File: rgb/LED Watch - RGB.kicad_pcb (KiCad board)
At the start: 4 copper layers, 42.9 x 50.3 mm, 146 parts, among them J1 AVR-ISP-6, J2 Lipo, J3 Coin Cell, SW1 SW_DPST, SW2 SW_DPST, U10 B39D3RGB-F6C0001HOU1930, U100 B39D3RGB-F6C0001HOU1930, U101 B39D3RGB-F6C0001HOU1930, U102 B39D3RGB-F6C0001HOU1930, U103 B39D3RGB-F6C0001HOU1930, U104 B39D3RGB-F6C0001HOU1930, U105 B39D3RGB-F6C0001HOU1930, U106 B39D3RGB-F6C0001HOU1930, U107 B39D3RGB-F6C0001HOU1930, U108 B39D3RGB-F6C0001HOU1930, U109 B39D3RGB-F6C0001HOU1930, U11 B39D3RGB-F6C0001HOU1930, U110 B39D3RGB-F6C0001HOU1930, U111 B39D3RGB-F6C0001HOU1930, U112 B39D3RGB-F6C0001HOU1930, U113 B39D3RGB-F6C0001HOU1930, U114 B39D3RGB-F6C0001HOU1930, U115 B39D3RGB-F6C0001HOU1930, U116 B39D3RGB-F6C0001HOU1930, U117 B39D3RGB-F6C0001HOU1930, U118 B39D3RGB-F6C0001HOU1930, U119 B39D3RGB-F6C0001HOU1930, U12 B39D3RGB-F6C0001HOU1930, U120 B39D3RGB-F6C0001HOU1930, U121 B39D3RGB-F6C0001HOU1930, U122 B39D3RGB-F6C0001HOU1930, U123 B39D3RGB-F6C0001HOU1930, U124 B39D3RGB-F6C0001HOU1930, U125 B39D3RGB-F6C0001HOU1930, U126 B39D3RGB-F6C0001HOU1930, U127 B39D3RGB-F6C0001HOU1930, U128 B39D3RGB-F6C0001HOU1930, U129 B39D3RGB-F6C0001HOU1930, U13 B39D3RGB-F6C0001HOU1930, U130 B39D3RGB-F6C0001HOU1930, U131 B39D3RGB-F6C0001HOU1930, U132 B39D3RGB-F6C0001HOU1930, U133 B39D3RGB-F6C0001HOU1930, U134 BMI160, U135 ATmega165PA-M, U14 B39D3RGB-F6C0001HOU1930, U15 B39D3RGB-F6C0001HOU1930, U16 B39D3RGB-F6C0001HOU1930, U17 B39D3RGB-F6C0001HOU1930, U18 B39D3RGB-F6C0001HOU1930, U19 B39D3RGB-F6C0001HOU1930, U2 B39D3RGB-F6C0001HOU1930, U20 B39D3RGB-F6C0001HOU1930, U21 B39D3RGB-F6C0001HOU1930, U22 B39D3RGB-F6C0001HOU1930, U23 B39D3RGB-F6C0001HOU1930, U24 B39D3RGB-F6C0001HOU1930, U25 B39D3RGB-F6C0001HOU1930, U26 B39D3RGB-F6C0001HOU1930, U27 B39D3RGB-F6C0001HOU1930, U28 B39D3RGB-F6C0001HOU1930, U29 B39D3RGB-F6C0001HOU1930, U3 B39D3RGB-F6C0001HOU1930, U30 B39D3RGB-F6C0001HOU1930, U31 B39D3RGB-F6C0001HOU1930, U32 B39D3RGB-F6C0001HOU1930, U33 B39D3RGB-F6C0001HOU1930, U34 B39D3RGB-F6C0001HOU1930, U35 B39D3RGB-F6C0001HOU1930, U36 B39D3RGB-F6C0001HOU1930, U37 B39D3RGB-F6C0001HOU1930, U38 B39D3RGB-F6C0001HOU1930, U39 B39D3RGB-F6C0001HOU1930, U4 B39D3RGB-F6C0001HOU1930, U40 B39D3RGB-F6C0001HOU1930, U41 B39D3RGB-F6C0001HOU1930, U42 B39D3RGB-F6C0001HOU1930, U43 B39D3RGB-F6C0001HOU1930, U44 B39D3RGB-F6C0001HOU1930, U45 B39D3RGB-F6C0001HOU1930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

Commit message: rgb: the live RGB work (Oct 2026 edits) becomes the main "LED Watch - RGB" project; add fab-rfq 2026-10-05, snapshots, Rhino layout
- rgb/LED Watch - RGB.* = the files from the working folder as of 2026-10-14 (board routes with 0 unconnected nets); the December 2025 version that the repository had is kept in rgb/archive/pre-claude/2025-12-08 ...
- rgb/production/fab-rfq 2026-10-05/ (BOM, placement files, Gerbers, DRC, quote screenshots, notes), rgb/archive/pre-claude/2026-10-05 snapshots ..., rgb/mechanical/watch layout 1.3dm
- updated KiCad project/layout state files of the archived variants from the working folder
- .gitignore: _old-desktop-copies/ (the previous loose Desktop copies, kept untouched next to the repository)

Co-Authored-By: Claude Sonnet 5.5 <noreply@anthropic.com>
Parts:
- U134: value BMI160 -> BMI270
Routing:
- net Net-(J1-VCC): track 42.8 -> 44.7 mm, vias 9 -> 11
- net /Minute6: track 32.9 -> 34.6 mm, vias 7 -> 8
- net Net-(J1-GND): vias 3 -> 7

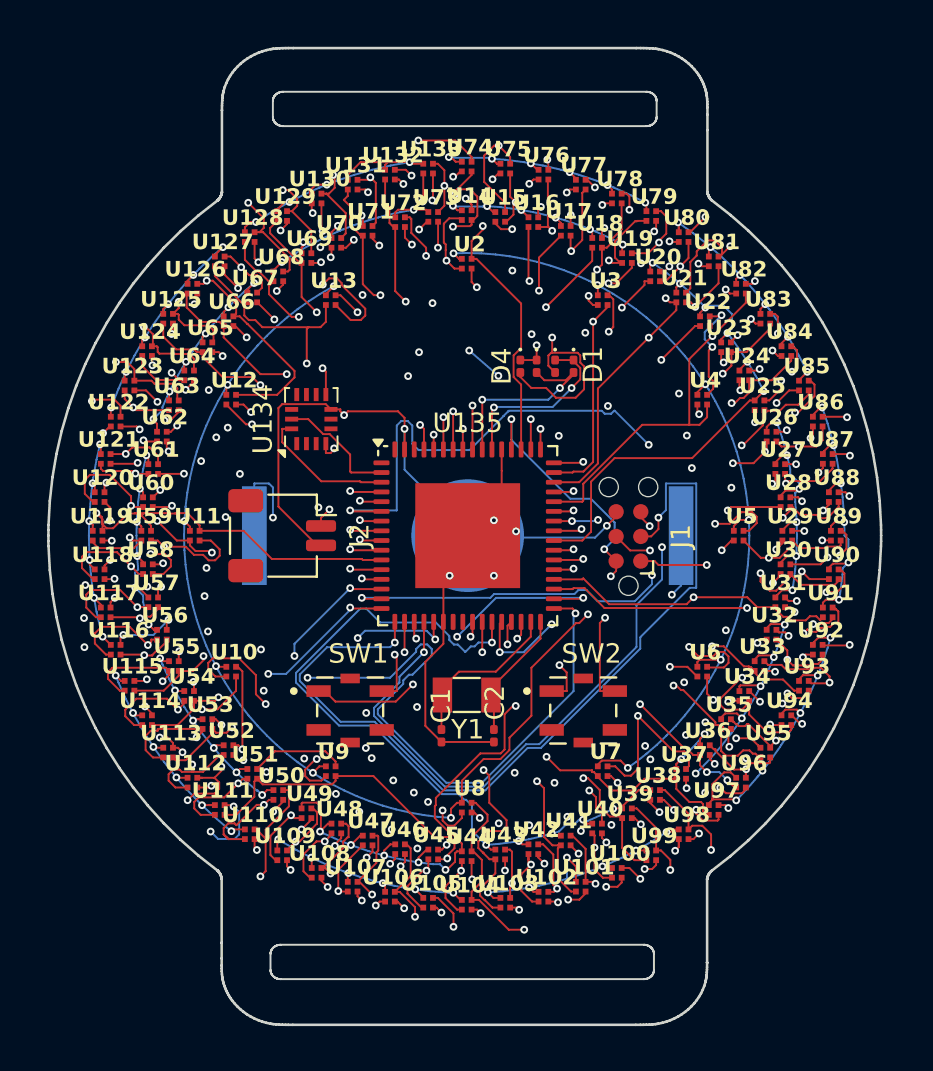
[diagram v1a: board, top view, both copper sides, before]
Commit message: rgb: the new RGB design takes over 'LED Watch - RGB'; the old routed RGB board (Harvatek, ATmega165PA) moves to rgb/archive; no 'v2' naming
Co-Authored-By: Claude Sonnet 5.5 <noreply@anthropic.com>
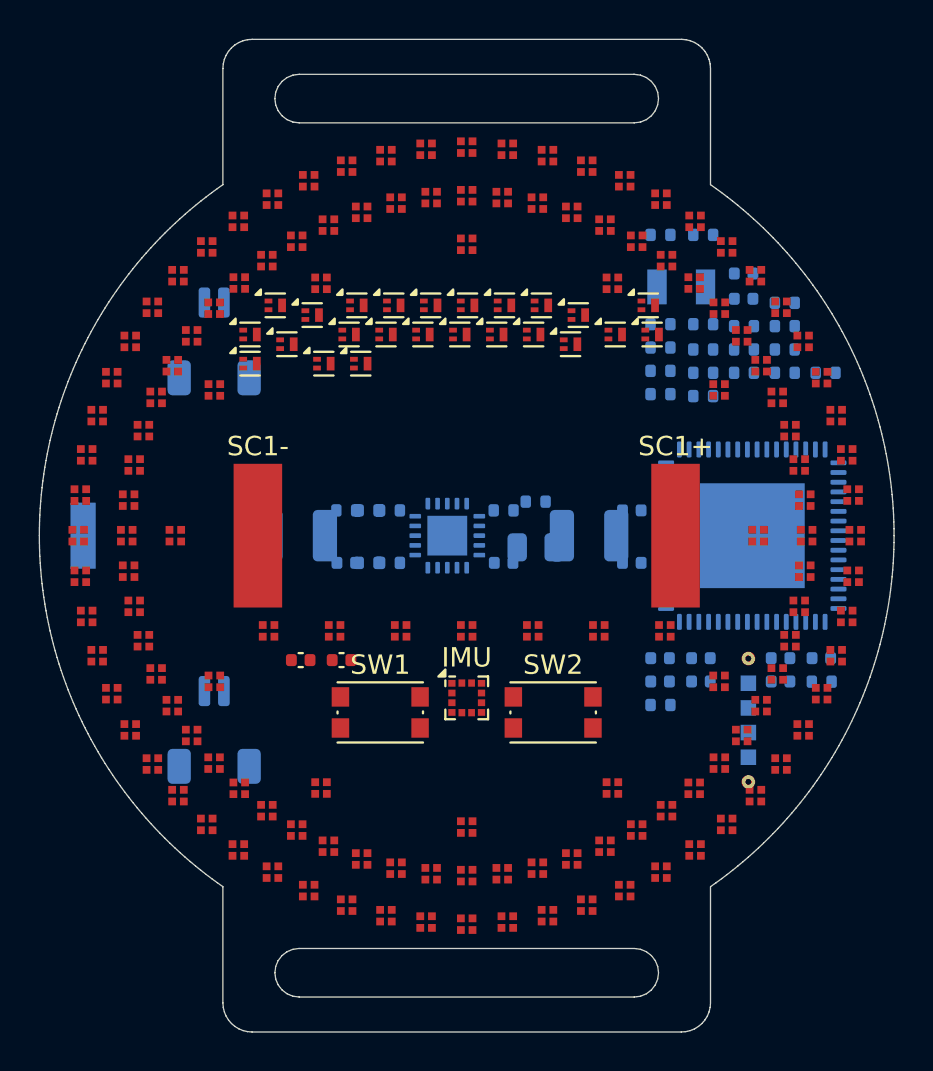
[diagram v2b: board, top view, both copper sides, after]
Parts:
- removed C1, C2: C, Capacitor_SMD:C_0201_0603Metric
- removed D1, D2, D3, D4: LED, LED_SMD:LED_0201_0603Metric
- removed J3: Coin Cell, Battery:BatteryHolder_Keystone_3034_1x20mm
- removed U134: BMI270, Package_LGA:Bosch_LGA-14_3x2.5mm_P0.5mm
- removed U135: ATmega165PA-M, Package_DFN_QFN:QFN-64-1EP_9x9mm_P0.5mm_EP5.4x5.4mm
- added BQ: BQ25570, BQ25570RGR_VQFN-20_3.5x3.5mm_P0.5mm_EP2.05mm, B.Cu at (99.0, 100.0)
- added BZ1: PKMCS0909E4000-R1, Piezo_Murata_PKMCS0909E4000-R1_9x9mm, B.Cu at (84.6, 100.0)
- added C20: 18p, C_0402_1005Metric, B.Cu at (114.3, 86.5)
- added C21: 18p, C_0402_1005Metric, B.Cu at (114.3, 87.8)
- added C30: 100n, C_0402_1005Metric, F.Cu at (91.5, 106.4)
- added C31: 100n, C_0402_1005Metric, F.Cu at (93.6, 106.4)
- added C50: 4u7, C_0402_1005Metric, B.Cu at (108.5, 98.7)
- added C51: 10n, C_0402_1005Metric, B.Cu at (93.8, 101.4)
- added C52: 4u7, C_0402_1005Metric, B.Cu at (101.9, 101.4)
- added C53: 10n, C_0402_1005Metric, B.Cu at (108.5, 101.4)
- added C54: 22u, C_0805_2012Metric, B.Cu at (103.5, 100.6)
- added CM1: 100n, C_0402_1005Metric, B.Cu at (110.0, 106.3)
- added CM2: 100n, C_0402_1005Metric, B.Cu at (112.1, 106.3)
- added CM3: 100n, C_0402_1005Metric, B.Cu at (116.2, 106.3)
- added CM4: 100n, C_0402_1005Metric, B.Cu at (118.3, 106.3)
- added CM5: 100n, C_0402_1005Metric, B.Cu at (110.0, 107.5)
- added CM6: 100n, C_0402_1005Metric, B.Cu at (112.1, 107.5)
- added CM7: 100n, C_0402_1005Metric, B.Cu at (116.2, 107.5)
- added IMU: LIS2DW12, LGA-12_2x2mm_P0.5mm, F.Cu at (100.0, 108.3)
- added IND1: NCD0808RGB1 / MHPA0808RGBDT, RGB0808_CommonAnode, F.Cu at (89.8, 104.9)
- added IND2: NCD0808RGB1 / MHPA0808RGBDT, RGB0808_CommonAnode, F.Cu at (93.2, 104.9)
- added IND3: NCD0808RGB1 / MHPA0808RGBDT, RGB0808_CommonAnode, F.Cu at (96.6, 104.9)
- added IND4: NCD0808RGB1 / MHPA0808RGBDT, RGB0808_CommonAnode, F.Cu at (100.0, 104.9)
- added IND5: NCD0808RGB1 / MHPA0808RGBDT, RGB0808_CommonAnode, F.Cu at (103.4, 104.9)
- added IND6: NCD0808RGB1 / MHPA0808RGBDT, RGB0808_CommonAnode, F.Cu at (106.8, 104.9)
- added IND7: NCD0808RGB1 / MHPA0808RGBDT, RGB0808_CommonAnode, F.Cu at (110.2, 104.9)
- added J1B: LiPo, JST_SH_SM02B-SRSS-TB_1x02-1MP_P1.00mm_Horizontal, B.Cu at (87.0, 110.0)
- added L1: 22uH, L_1210_3225Metric, B.Cu at (106.3, 100.0)
- added L2: 10uH, L_1210_3225Metric, B.Cu at (91.3, 100.0)
- added MCU: AVR128DB64-I/MR, VQFN-64-1EP_9x9mm_P0.5mm_EP5.4x5.4mm, B.Cu at (114.7, 100.0)
- added Q1: DMP21D0UFB4, Diodes_DFN1006-3, F.Cu at (90.1, 88.1)
- added Q10: DMP21D0UFB4, Diodes_DFN1006-3, F.Cu at (105.7, 88.6)
- added Q11: DMP21D0UFB4, Diodes_DFN1006-3, F.Cu at (88.8, 89.6)
- added Q12: DMP21D0UFB4, Diodes_DFN1006-3, F.Cu at (93.9, 89.6)
- added Q13: DMP21D0UFB4, Diodes_DFN1006-3, F.Cu at (95.8, 89.6)
- added Q14: DMP21D0UFB4, Diodes_DFN1006-3, F.Cu at (97.7, 89.6)
- added Q15: DMP21D0UFB4, Diodes_DFN1006-3, F.Cu at (99.6, 89.6)
- added Q16: DMP21D0UFB4, Diodes_DFN1006-3, F.Cu at (101.5, 89.6)
- added Q17: DMP21D0UFB4, Diodes_DFN1006-3, F.Cu at (103.4, 89.6)
- added Q18: DMP21D0UFB4, Diodes_DFN1006-3, F.Cu at (107.6, 89.6)
- added Q19: DMP21D0UFB4, Diodes_DFN1006-3, F.Cu at (109.5, 89.6)
- added Q2: DMP21D0UFB4, Diodes_DFN1006-3, F.Cu at (94.3, 88.1)
- added Q20: DMP21D0UFB4, Diodes_DFN1006-3, F.Cu at (90.7, 90.1)
- added Q21: DMP21D0UFB4, Diodes_DFN1006-3, F.Cu at (105.3, 90.1)
- added Q22: DMP21D0UFB4, Diodes_DFN1006-3, F.Cu at (88.8, 91.1)
- added Q23: DMP21D0UFB4, Diodes_DFN1006-3, F.Cu at (92.6, 91.1)
- added Q24: DMP21D0UFB4, Diodes_DFN1006-3, F.Cu at (94.5, 91.1)
- added Q3: DMP21D0UFB4, Diodes_DFN1006-3, F.Cu at (96.2, 88.1)
- added Q4: DMP21D0UFB4, Diodes_DFN1006-3, F.Cu at (98.1, 88.1)
- added Q5: DMP21D0UFB4, Diodes_DFN1006-3, F.Cu at (100.0, 88.1)
- added Q6: DMP21D0UFB4, Diodes_DFN1006-3, F.Cu at (101.9, 88.1)
- added Q7: DMP21D0UFB4, Diodes_DFN1006-3, F.Cu at (103.8, 88.1)
- added Q8: DMP21D0UFB4, Diodes_DFN1006-3, F.Cu at (109.3, 88.1)
- added Q9: DMP21D0UFB4, Diodes_DFN1006-3, F.Cu at (92.0, 88.6)
- added R20: 10k, R_0402_1005Metric, B.Cu at (118.3, 107.5)
- added R21: 10k, R_0402_1005Metric, B.Cu at (110.0, 108.7)
- added R50: 6.49M, R_0402_1005Metric, B.Cu at (96.0, 101.4)
- added R51: 5.11M, R_0402_1005Metric, B.Cu at (95.0, 101.4)
- added R52: 1.47M, R_0402_1005Metric, B.Cu at (96.0, 98.7)
- added R53: 6.49M, R_0402_1005Metric, B.Cu at (103.5, 98.2)
- added R54: 3.74M, R_0402_1005Metric, B.Cu at (101.9, 98.7)
- added R55: 6.49M, R_0402_1005Metric, B.Cu at (93.8, 98.7)
- added R56: 3.74M, R_0402_1005Metric, B.Cu at (95.0, 98.7)
- added RC1: R, R_0402_1005Metric, B.Cu at (110.0, 84.5)
- added RC10: R, R_0402_1005Metric, B.Cu at (114.3, 90.4)
- added RC11: R, R_0402_1005Metric, B.Cu at (116.4, 90.4)
- added RC12: R, R_0402_1005Metric, B.Cu at (110.0, 91.5)
- added RC13: R, R_0402_1005Metric, B.Cu at (112.2, 91.6)
- added RC14: R, R_0402_1005Metric, B.Cu at (114.3, 91.6)
- added RC15: R, R_0402_1005Metric, B.Cu at (116.4, 91.6)
- added RC16: R, R_0402_1005Metric, B.Cu at (118.5, 91.6)
- added RC17: R, R_0402_1005Metric, B.Cu at (110.0, 92.7)
- added RC18: R, R_0402_1005Metric, B.Cu at (112.2, 92.8)
- added RC2: R, R_0402_1005Metric, B.Cu at (112.2, 84.5)
- added RC3: R, R_0402_1005Metric, B.Cu at (116.4, 88.0)
- added RC4: R, R_0402_1005Metric, B.Cu at (110.0, 89.1)
- added RC5: R, R_0402_1005Metric, B.Cu at (112.2, 89.1)
- added RC6: R, R_0402_1005Metric, B.Cu at (114.3, 89.2)
- added RC7: R, R_0402_1005Metric, B.Cu at (116.4, 89.2)
- added RC8: R, R_0402_1005Metric, B.Cu at (110.0, 90.3)
- added RC9: R, R_0402_1005Metric, B.Cu at (112.2, 90.4)
- added SC1+: cell pad, KXOB25_cell_pad_2.5x7.4mm, F.Cu at (110.8, 100.0)
- added SC1-: cell pad, KXOB25_cell_pad_2.5x7.4mm, F.Cu at (89.2, 100.0)
- J1: value AVR-ISP-6 -> LiPo; footprint Connector:Tag-Connect_TC2030-IDC-NL_2x03_P1.27mm_Vertical -> JST_SH_SM02B-SRSS-TB_1x02-1MP_P1.00mm_Horizontal; moved to B.Cu
- J2: value Lipo -> UPDI pogo; footprint Connector_JST:JST_SH_SM02B-SRSS-TB_1x02-1MP_P1.00mm_Horizontal -> UPDI_Pogo_1x4_P1.27mm_2Guide; moved to B.Cu
- SW1, SW2: value SW_DPST -> SW; footprint kicad-footprints:SW_TS21-34-035-BK-260-SMT-TR -> SW_Push_1P1T_NO_CK_KMR2
- U10, U100, U101, U102, U103, U104, U105, U106, U107, U108, U109, U11, U110, U111, U112, U113, U114, U115, U116, U117, U118, U119, U12, U120, U121, U122, U123, U124, U125, U126, U127, U128, U129, U13, U130, U131, U132, U133, U14, U15, U16, U17, U18, U19, U2, U20, U21, U22, U23, U24, U25, U26, U27, U28, U29, U3, U30, U31, U32, U33, U34, U35, U36, U37, U38, U39, U4, U40, U41, U42, U43, U44, U45, U46, U47, U48, U49, U5, U50, U51, U52, U53, U54, U55, U56, U57, U58, U59, U6, U60, U61, U62, U63, U64, U65, U66, U67, U68, U69, U7, U70, U71, U72, U73, U74, U75, U76, U77, U78, U79, U8, U80, U81, U82, U83, U84, U85, U86, U87, U88, U89, U9, U90, U91, U92, U93, U94, U95, U96, U97, U98, U99: value B39D3RGB-F6C0001HOU1930 -> NCD0808RGB1 / MHPA0808RGBDT; footprint B39D3RGB_F6C0001HOU1930:B39D3RGB-F6C0001HOU1930_HVK -> RGB0808_CommonAnode
- Y1: value Crystal -> 32.768kHz; footprint Crystal:Crystal_SMD_3215-2Pin_3.2x1.5mm -> Crystal_SMD_3215-2Pin_3.2x1.5mm; moved to B.Cu
- moved J2 25.8 mm to (114.5, 109.5), turned to 90 degrees
- moved Y1 23.7 mm to (111.0, 87.2)
- moved J1 23.6 mm to (87.0, 90.0), turned to 180 degrees
- moved SW1 1.55 mm to (95.5, 109.1)
- moved SW2 1.55 mm to (104.5, 109.1)
- moved U126 1.00 mm to (85.1, 86.6), turned to 90 degrees
- moved U127 1.00 mm to (86.6, 85.1), turned to 90 degrees
- moved U65 1.00 mm to (85.8, 89.7), turned to 90 degrees
- moved U68 1.00 mm to (89.7, 85.8), turned to 90 degrees
- moved U66 1.00 mm to (87.0, 88.3), turned to 90 degrees
- moved U67 1.00 mm to (88.3, 87.0), turned to 90 degrees
- moved U10 1.00 mm to (87.0, 107.5), turned to 90 degrees
- moved U12 1.00 mm to (87.0, 92.5), turned to 90 degrees
- moved U13 1.00 mm to (92.5, 87.0), turned to 90 degrees
- moved U3 1.00 mm to (107.5, 87.0), turned to 90 degrees
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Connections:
- J1 pad 1: /B5 -> (no net)
- J1 pad 2: Net-(J1-VCC) -> (no net)
- J2 pad 1: Net-(J1-VCC) -> (no net)
- J2 pad 2: Net-(J1-GND) -> (no net)
- SW1 pad 1: Net-(U135-PF0) -> (no net)
- SW1 pad 2: Net-(U135-PF1) -> (no net)
- SW2 pad 1: Net-(U135-PF2) -> (no net)
- SW2 pad 2: Net-(U135-PF3) -> (no net)
- U10 pad 2: /B3 -> /R3
- U10 pad 4: /R3 -> /B3
- U100 pad 2: /B3 -> /R3
- U100 pad 4: /R3 -> /B3
- U101 pad 2: /B4 -> /R4
- U101 pad 4: /R4 -> /B4
- U102 pad 2: /B5 -> /R5
- U102 pad 4: /R5 -> /B5
- U103 pad 2: /B6 -> /R6
- U103 pad 4: /R6 -> /B6
- U104 pad 2: /B1 -> /R1
- U104 pad 4: /R1 -> /B1
- U105 pad 2: /B2 -> /R2
- U105 pad 4: /R2 -> /B2
- U106 pad 2: /B3 -> /R3
- U106 pad 4: /R3 -> /B3
- U107 pad 2: /B4 -> /R4
- U107 pad 4: /R4 -> /B4
- U108 pad 2: /B5 -> /R5
- U108 pad 4: /R5 -> /B5
- U109 pad 2: /B6 -> /R6
- U109 pad 4: /R6 -> /B6
- U11 pad 2: /B4 -> /R4
- U11 pad 4: /R4 -> /B4
- U110 pad 2: /B1 -> /R1
- U110 pad 4: /R1 -> /B1
- U111 pad 2: /B2 -> /R2
- U111 pad 4: /R2 -> /B2
- U112 pad 2: /B3 -> /R3
- U112 pad 4: /R3 -> /B3
- U113 pad 2: /B4 -> /R4
- U113 pad 4: /R4 -> /B4
- U114 pad 2: /B5 -> /R5
- U114 pad 4: /R5 -> /B5
- U115 pad 2: /B6 -> /R6
- U115 pad 4: /R6 -> /B6
- U116 pad 2: /B1 -> /R1
- U116 pad 4: /R1 -> /B1
- U117 pad 2: /B2 -> /R2
- U117 pad 4: /R2 -> /B2
- U118 pad 2: /B3 -> /R3
- U118 pad 4: /R3 -> /B3
- U119 pad 2: /B4 -> /R4
- U119 pad 4: /R4 -> /B4
- U12 pad 2: /B5 -> /R5
- U12 pad 4: /R5 -> /B5
- U120 pad 2: /B5 -> /R5
- U120 pad 4: /R5 -> /B5
- U121 pad 2: /B6 -> /R6
- U121 pad 4: /R6 -> /B6
- U122 pad 2: /B1 -> /R1
- U122 pad 4: /R1 -> /B1
- U123 pad 2: /B2 -> /R2
- U123 pad 4: /R2 -> /B2
- U124 pad 2: /B3 -> /R3
- U124 pad 4: /R3 -> /B3
- U125 pad 2: /B4 -> /R4
- U125 pad 4: /R4 -> /B4
- U126 pad 2: /B5 -> /R5
- U126 pad 4: /R5 -> /B5
- U127 pad 2: /B6 -> /R6
- U127 pad 4: /R6 -> /B6
- U128 pad 2: /B1 -> /R1
- U128 pad 4: /R1 -> /B1
- U129 pad 2: /B2 -> /R2
- U129 pad 4: /R2 -> /B2
- U13 pad 2: /B6 -> /R6
- U13 pad 4: /R6 -> /B6
- U130 pad 2: /B3 -> /R3
- U130 pad 4: /R3 -> /B3
- U131 pad 2: /B4 -> /R4
- U131 pad 4: /R4 -> /B4
- U132 pad 2: /B5 -> /R5
- U132 pad 4: /R5 -> /B5
- U133 pad 2: /B6 -> /R6
- U133 pad 4: /R6 -> /B6
- U14 pad 2: /B1 -> /R1
- U14 pad 4: /R1 -> /B1
- U15 pad 2: /B2 -> /R2
- U15 pad 4: /R2 -> /B2
- U16 pad 2: /B3 -> /R3
- U16 pad 4: /R3 -> /B3
- U17 pad 2: /B4 -> /R4
- U17 pad 4: /R4 -> /B4
- U18 pad 2: /B5 -> /R5
- U18 pad 4: /R5 -> /B5
- U19 pad 2: /B6 -> /R6
- U19 pad 4: /R6 -> /B6
- U2 pad 2: /B1 -> /R1
- U2 pad 4: /R1 -> /B1
- U20 pad 2: /B1 -> /R1
- U20 pad 4: /R1 -> /B1
- U21 pad 2: /B2 -> /R2
- U21 pad 4: /R2 -> /B2
- U22 pad 2: /B3 -> /R3
- U22 pad 4: /R3 -> /B3
- U23 pad 2: /B4 -> /R4
- U23 pad 4: /R4 -> /B4
- U24 pad 2: /B5 -> /R5
- U24 pad 4: /R5 -> /B5
- U25 pad 2: /B6 -> /R6
- U25 pad 4: /R6 -> /B6
- U26 pad 2: /B1 -> /R1
- U26 pad 4: /R1 -> /B1
- U27 pad 2: /B2 -> /R2
- U27 pad 4: /R2 -> /B2
- U28 pad 2: /B3 -> /R3
- U28 pad 4: /R3 -> /B3
- U29 pad 2: /B4 -> /R4
- U29 pad 4: /R4 -> /B4
- U3 pad 2: /B2 -> /R2
- U3 pad 4: /R2 -> /B2
- U30 pad 2: /B5 -> /R5
- U30 pad 4: /R5 -> /B5
- U31 pad 2: /B6 -> /R6
- U31 pad 4: /R6 -> /B6
- U32 pad 2: /B1 -> /R1
- U32 pad 4: /R1 -> /B1
- U33 pad 2: /B2 -> /R2
- U33 pad 4: /R2 -> /B2
- U34 pad 2: /B3 -> /R3
- U34 pad 4: /R3 -> /B3
- U35 pad 2: /B4 -> /R4
- U35 pad 4: /R4 -> /B4
- U36 pad 2: /B5 -> /R5
- U36 pad 4: /R5 -> /B5
- U37 pad 2: /B6 -> /R6
- U37 pad 4: /R6 -> /B6
- U38 pad 2: /B1 -> /R1
- U38 pad 4: /R1 -> /B1
- U39 pad 2: /B2 -> /R2
- U39 pad 4: /R2 -> /B2
- U4 pad 2: /B3 -> /R3
- U4 pad 4: /R3 -> /B3
- U40 pad 2: /B3 -> /R3
- U40 pad 4: /R3 -> /B3
- U41 pad 2: /B4 -> /R4
- U41 pad 4: /R4 -> /B4
- U42 pad 2: /B5 -> /R5
- U42 pad 4: /R5 -> /B5
- U43 pad 2: /B6 -> /R6
- U43 pad 4: /R6 -> /B6
- U44 pad 2: /B1 -> /R1
- U44 pad 4: /R1 -> /B1
- U45 pad 2: /B2 -> /R2
- U45 pad 4: /R2 -> /B2
- U46 pad 2: /B3 -> /R3
- U46 pad 4: /R3 -> /B3
- U47 pad 2: /B4 -> /R4
- U47 pad 4: /R4 -> /B4
- U48 pad 2: /B5 -> /R5
- U48 pad 4: /R5 -> /B5
- U49 pad 2: /B6 -> /R6
- U49 pad 4: /R6 -> /B6
- U5 pad 2: /B4 -> /R4
- U5 pad 4: /R4 -> /B4
- U50 pad 2: /B1 -> /R1
- U50 pad 4: /R1 -> /B1
- U51 pad 2: /B2 -> /R2
- U51 pad 4: /R2 -> /B2
- U52 pad 2: /B3 -> /R3
- U52 pad 4: /R3 -> /B3
- U53 pad 2: /B4 -> /R4
- U53 pad 4: /R4 -> /B4
- U54 pad 2: /B5 -> /R5
- U54 pad 4: /R5 -> /B5
- U55 pad 2: /B6 -> /R6
- U55 pad 4: /R6 -> /B6
- U56 pad 2: /B1 -> /R1
- U56 pad 4: /R1 -> /B1
- U57 pad 2: /B2 -> /R2
- U57 pad 4: /R2 -> /B2
- U58 pad 2: /B3 -> /R3
- U58 pad 4: /R3 -> /B3
- U59 pad 2: /B4 -> /R4
- U59 pad 4: /R4 -> /B4
- U6 pad 2: /B5 -> /R5
- U6 pad 4: /R5 -> /B5
- U60 pad 2: /B5 -> /R5
- U60 pad 4: /R5 -> /B5
- U61 pad 2: /B6 -> /R6
- U61 pad 4: /R6 -> /B6
- U62 pad 2: /B1 -> /R1
- U62 pad 4: /R1 -> /B1
- U63 pad 2: /B2 -> /R2
- U63 pad 4: /R2 -> /B2
- U64 pad 2: /B3 -> /R3
- U64 pad 4: /R3 -> /B3
- U65 pad 2: /B4 -> /R4
- U65 pad 4: /R4 -> /B4
- U66 pad 2: /B5 -> /R5
- U66 pad 4: /R5 -> /B5
- U67 pad 2: /B6 -> /R6
- U67 pad 4: /R6 -> /B6
- U68 pad 2: /B1 -> /R1
- U68 pad 4: /R1 -> /B1
- U69 pad 2: /B2 -> /R2
- U69 pad 4: /R2 -> /B2
- U7 pad 2: /B6 -> /R6
- U7 pad 4: /R6 -> /B6
- U70 pad 2: /B3 -> /R3
- U70 pad 4: /R3 -> /B3
- U71 pad 2: /B4 -> /R4
- U71 pad 4: /R4 -> /B4
- U72 pad 2: /B5 -> /R5
- U72 pad 4: /R5 -> /B5
- U73 pad 2: /B6 -> /R6
- U73 pad 4: /R6 -> /B6
- U74 pad 2: /B1 -> /R1
- U74 pad 4: /R1 -> /B1
- U75 pad 2: /B2 -> /R2
- U75 pad 4: /R2 -> /B2
- U76 pad 2: /B3 -> /R3
- U76 pad 4: /R3 -> /B3
- U77 pad 2: /B4 -> /R4
- U77 pad 4: /R4 -> /B4
- U78 pad 2: /B5 -> /R5
- U78 pad 4: /R5 -> /B5
- U79 pad 2: /B6 -> /R6
- U79 pad 4: /R6 -> /B6
- U8 pad 2: /B1 -> /R1
- U8 pad 4: /R1 -> /B1
- U80 pad 2: /B1 -> /R1
- U80 pad 4: /R1 -> /B1
- U81 pad 2: /B2 -> /R2
- U81 pad 4: /R2 -> /B2
- U82 pad 2: /B3 -> /R3
- U82 pad 4: /R3 -> /B3
- U83 pad 2: /B4 -> /R4
- U83 pad 4: /R4 -> /B4
- U84 pad 2: /B5 -> /R5
- U84 pad 4: /R5 -> /B5
- U85 pad 2: /B6 -> /R6
- U85 pad 4: /R6 -> /B6
- U86 pad 2: /B1 -> /R1
- U86 pad 4: /R1 -> /B1
- U87 pad 2: /B2 -> /R2
- U87 pad 4: /R2 -> /B2
- U88 pad 2: /B3 -> /R3
- U88 pad 4: /R3 -> /B3
- U89 pad 2: /B4 -> /R4
- U89 pad 4: /R4 -> /B4
- U9 pad 2: /B2 -> /R2
- U9 pad 4: /R2 -> /B2
- U90 pad 2: /B5 -> /R5
- U90 pad 4: /R5 -> /B5
- U91 pad 2: /B6 -> /R6
- U91 pad 4: /R6 -> /B6
- U92 pad 2: /B1 -> /R1
- U92 pad 4: /R1 -> /B1
- U93 pad 2: /B2 -> /R2
- U93 pad 4: /R2 -> /B2
- U94 pad 2: /B3 -> /R3
- U94 pad 4: /R3 -> /B3
- U95 pad 2: /B4 -> /R4
- U95 pad 4: /R4 -> /B4
- U96 pad 2: /B5 -> /R5
- U96 pad 4: /R5 -> /B5
- U97 pad 2: /B6 -> /R6
- U97 pad 4: /R6 -> /B6
- U98 pad 2: /B1 -> /R1
- U98 pad 4: /R1 -> /B1
- U99 pad 2: /B2 -> /R2
- U99 pad 4: /R2 -> /B2
- Y1 pad 1: Net-(U135-PD6) -> (no net)
- Y1 pad 2: Net-(U135-PD7) -> (no net)
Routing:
- net /R6: track 237.2 -> 0.00 mm, vias 19 -> 0
- net /R1: track 208.9 -> 0.00 mm, vias 18 -> 0
- net /R3: track 208.3 -> 0.00 mm, vias 21 -> 0
- net /R2: track 205.0 -> 0.00 mm, vias 19 -> 0
- net /R5: track 197.4 -> 0.00 mm, vias 20 -> 0
- net /B3: track 185.0 -> 0.00 mm, vias 25 -> 0
- net /R4: track 184.1 -> 0.00 mm, vias 16 -> 0
- net /B5: track 179.5 -> 0.00 mm, vias 24 -> 0
- net /G5: track 179.2 -> 0.00 mm, vias 25 -> 0
- net /B4: track 178.5 -> 0.00 mm, vias 20 -> 0
- net /B2: track 178.0 -> 0.00 mm, vias 21 -> 0
- net /B6: track 175.6 -> 0.00 mm, vias 18 -> 0
- net /G2: track 174.8 -> 0.00 mm, vias 19 -> 0
- net /B1: track 173.6 -> 0.00 mm, vias 24 -> 0
- net /G6: track 168.4 -> 0.00 mm, vias 24 -> 0
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- removed copper zone on In1.Cu, net Net-(J1-GND)
- removed copper zone on In2.Cu, net Net-(J1-VCC)
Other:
- board size 42.9 x 50.3 mm -> 44 x 51.1 mm

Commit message: rgb: LEDs turned radially like the single-colour ring; MCU-on-front study and two front-MCU variant boards (DB48 + shift registers, DB64 with the cell shifted); build_sketch --variant
Co-Authored-By: Claude Sonnet 5.5 <noreply@anthropic.com>
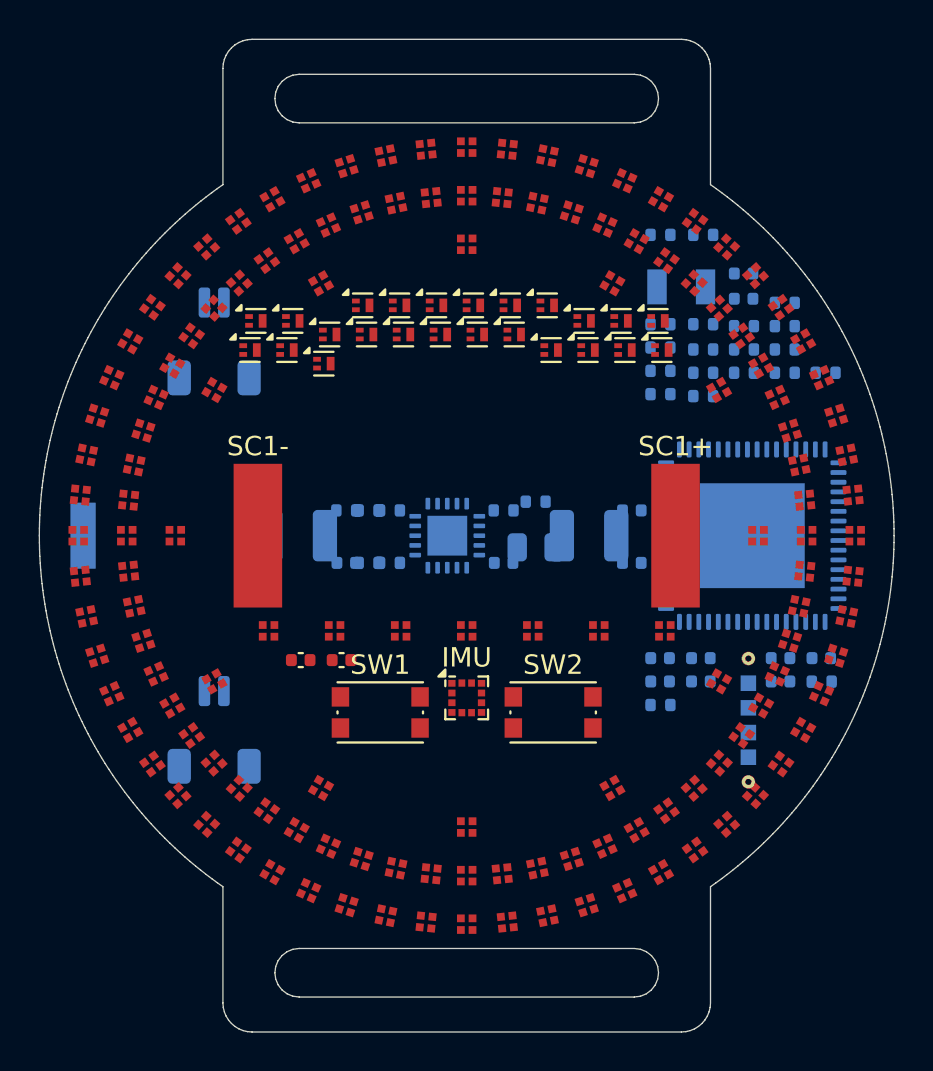
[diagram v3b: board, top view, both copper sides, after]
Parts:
- moved Q11 21.0 mm to (109.8, 88.9)
- moved Q22 19.3 mm to (108.1, 90.4)
- moved Q19 18.8 mm to (90.7, 90.4)
- moved Q18 18.8 mm to (88.8, 90.4)
- moved Q8 18.3 mm to (91.0, 88.9)
- moved Q23 17.4 mm to (110.0, 90.4)
- moved Q7 14.7 mm to (89.1, 88.9)
- moved Q9 14.0 mm to (106.0, 88.9)
- moved Q20 13.6 mm to (104.3, 90.4)
- moved Q1 4.50 mm to (94.6, 88.1)
- moved Q10 2.22 mm to (107.9, 88.9)
- moved Q2 2.20 mm to (96.5, 88.1)
- moved Q4 2.20 mm to (100.3, 88.1)
- moved Q5 2.20 mm to (102.2, 88.1)
- moved Q6 2.20 mm to (104.1, 88.1)
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
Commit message: rgb: column resistors in the hour-ring gaps (default), option for the row switches too, exact courtyard check, variant board and pictures
Co-Authored-By: Claude Sonnet 5.5 <noreply@anthropic.com>
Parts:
- RC1, RC10, RC11, RC12, RC13, RC14, RC15, RC16, RC17, RC18, RC2, RC3, RC4, RC5, RC6, RC7, RC8, RC9: moved to F.Cu
- moved RC7 32.4 mm to (96.1, 114.5), turned to -105 degrees
- moved RC9 29.9 mm to (85.5, 103.9), turned to -165 degrees
- moved RC10 29.3 mm to (85.5, 96.1), turned to 165 degrees
- moved RC8 28.9 mm to (89.4, 110.6), turned to -135 degrees
- moved RC11 27.0 mm to (89.4, 89.4), turned to 135 degrees
- moved RC6 26.9 mm to (104.5, 114.3), turned to -72.651 degrees
- moved RC18 23.6 mm to (103.3, 114.6), turned to -77.349 degrees
- moved RC5 21.1 mm to (111.0, 110.2), turned to -42.651 degrees
- moved RC17 18.3 mm to (110.2, 111.0), turned to -47.349 degrees
- moved Q19 17.8 mm to (108.5, 90.8)
- moved Q18 17.8 mm to (106.6, 90.4)
- moved RC12 15.1 mm to (96.1, 85.5), turned to 105 degrees
- moved Q8 15.0 mm to (106.0, 88.9)
- moved RC4 14.9 mm to (114.6, 103.3), turned to -12.651 degrees
- moved Q10 14.6 mm to (93.3, 89.6)
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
